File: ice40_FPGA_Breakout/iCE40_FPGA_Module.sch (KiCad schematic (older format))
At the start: 100 parts, among them U1 iCE40HX8_CT256

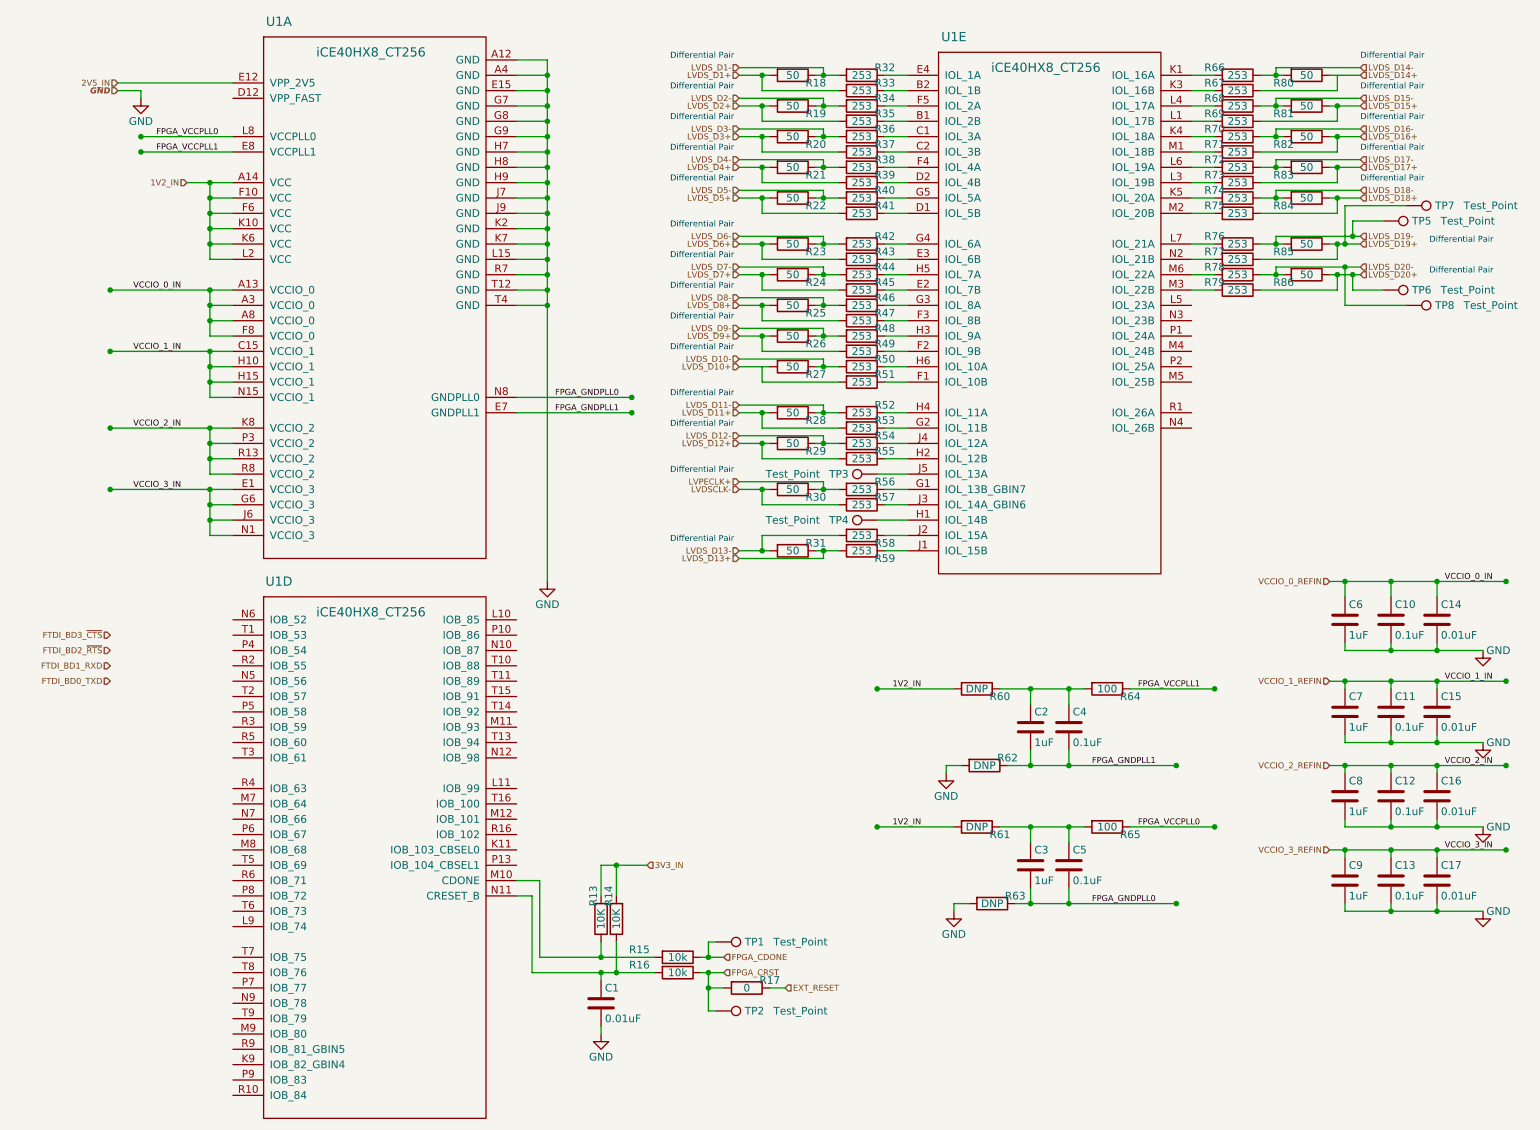
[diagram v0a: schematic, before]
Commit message: schematic clean up, label aligned
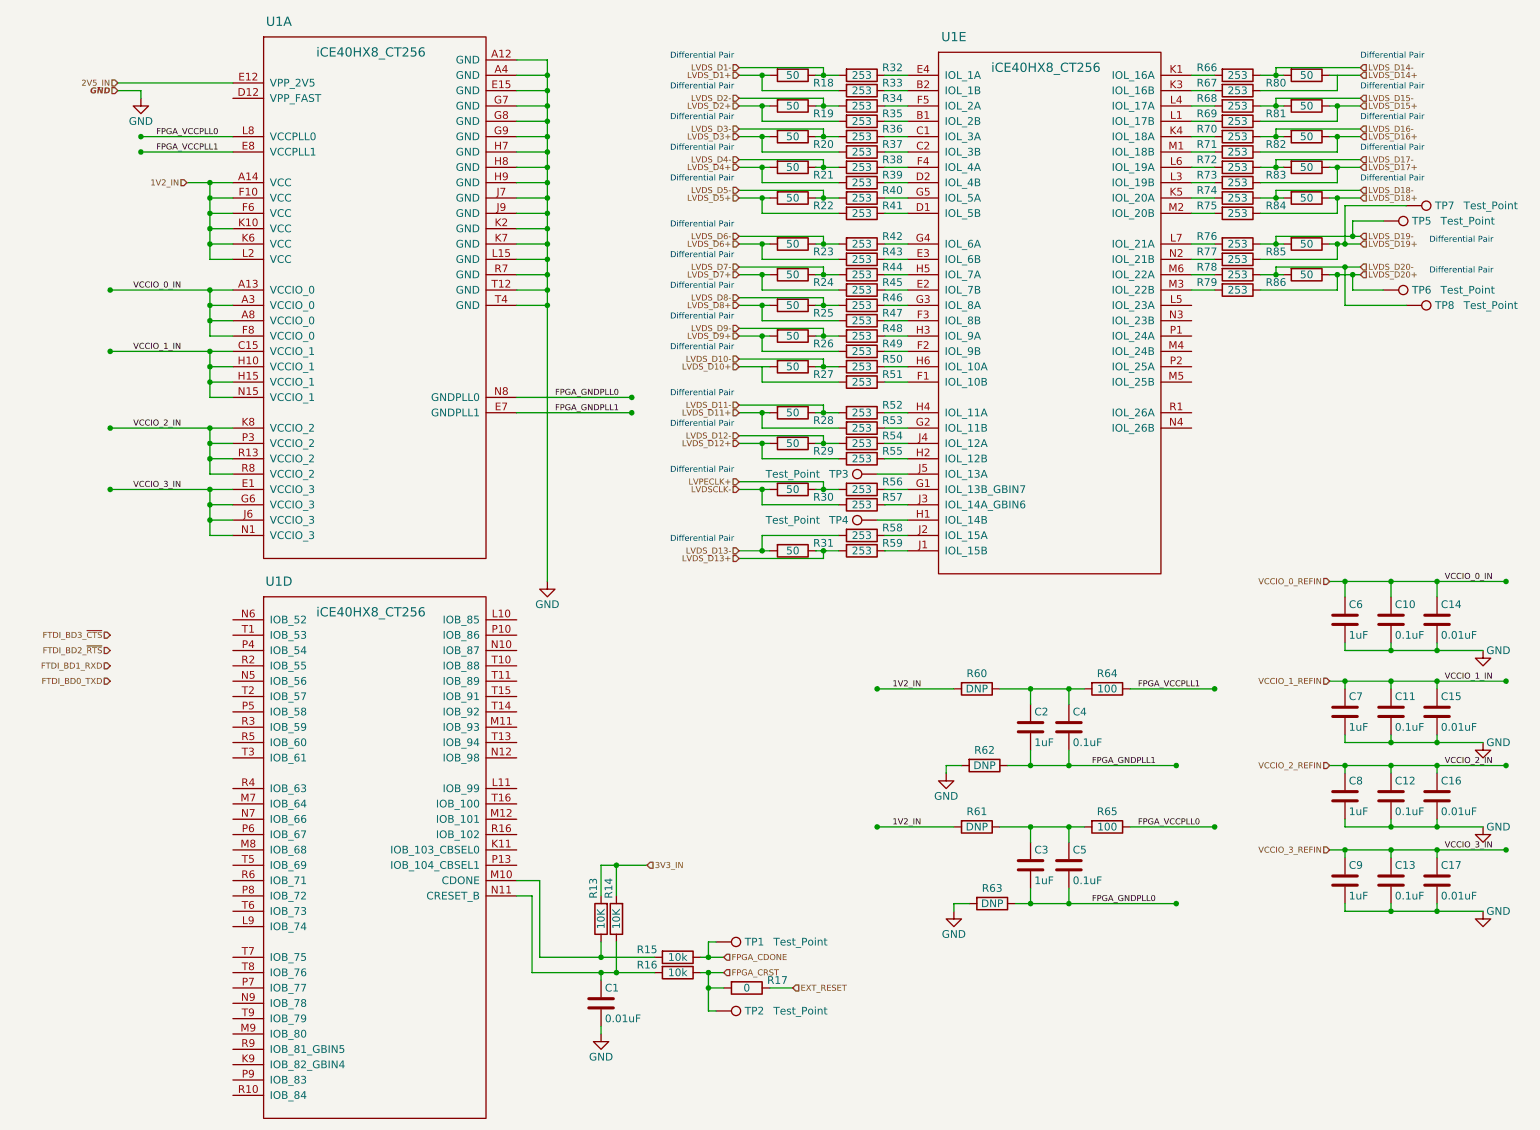
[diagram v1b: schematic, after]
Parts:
- C1, C10, C11, C12, C13, C14, C15, C16, C17, C4, C5: footprint (none) -> Capacitor_SMD:C_0402_1005Metric
- C2, C3, C6, C7, C8, C9: footprint (none) -> Capacitor_SMD:C_0603_1608Metric
- R13, R14, R15, R16, R17, R18, R19, R20, R21, R22, R23, R24, R25, R26, R27, R28, R29, R30, R31, R32, R33, R34, R35, R36, R37, R38, R39, R40, R41, R42, R43, R44, R45, R46, R47, R48, R49, R50, R51, R52, R53, R54, R55, R56, R57, R58, R59, R66, R67, R68, R69, R70, R71, R72, R73, R74, R75, R76, R77, R78, R79, R80, R81, R82, R83, R84, R85, R86: footprint (none) -> Resistor_SMD:R_0402_1005Metric
- R60, R61, R62, R63, R64, R65: footprint (none) -> Resistor_SMD:R_0603_1608Metric
- TP1, TP2, TP3, TP4, TP5, TP6, TP7, TP8: footprint (none) -> Conn_PinHeader_2.00mm:PinHeader_1x01_P2.00mm_Vertical

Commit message: assigned footprint to each component
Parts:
- TP1: footprint Conn_PinHeader_2.00mm:PinHeader_1x01_P2.00mm_Vertical -> TestPoint:TestPoint_Plated_Hole_D2.0mm
- TP2, TP3, TP4, TP5, TP6, TP7, TP8: footprint Conn_PinHeader_2.00mm:PinHeader_1x01_P2.00mm_Vertical -> TestPoint:TestPoint_Pad_D2.0mm
- U1: footprint (none) -> GTI_Footprint_Lib:BGA-256_12mmx12mm_Layout_14mmx14mm_P0.8mm_R0.5mm
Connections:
- net LVDS_D14+: now also R67.1

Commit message: , diff pair, memory and power component grouping
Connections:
- net LVDS_D10+: now also R51.2
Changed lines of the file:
@@
 $EndComp
 $Comp
-L GND #PWR02
+L GND #PWR3
 U 1 1 5A263712
 P 4800 4150
-F 0 "#PWR02" H 4800 3900 50  0001 C CNN
+F 0 "#PWR3" H 4800 3900 50  0001 C CNN
 F 1 "GND" H 4800 4000 50  0000 C CNN
 F 2 "" H 4800 4150 50  0001 C CNN
@@
 $EndComp
 $Comp
-L GND #PWR03
+L GND #PWR6
 U 1 1 5A3E2FC7
 P 7450 6300
-F 0 "#PWR03" H 7450 6050 50  0001 C CNN
+F 0 "#PWR6" H 7450 6050 50  0001 C CNN
 F 1 "GND" H 7450 6150 50  0000 C CNN
 F 2 "" H 7450 6300 50  0001 C CNN
@@
 $EndComp
 $Comp
-L GND #PWR04
+L GND #PWR5
 U 1 1 5A3E512A
 P 7400 5400
-F 0 "#PWR04" H 7400 5150 50  0001 C CNN
+F 0 "#PWR5" H 7400 5150 50  0001 C CNN
 F 1 "GND" H 7400 5250 50  0000 C CNN
 F 2 "" H 7400 5400 50  0001 C CNN
@@
 $EndComp
 $Comp
-L GND #PWR05
+L GND #PWR10
 U 1 1 5A407417
 P 10900 6300
-F 0 "#PWR05" H 10900 6050 50  0001 C CNN
+F 0 "#PWR10" H 10900 6050 50  0001 C CNN
 F 1 "GND" H 11000 6300 50  0000 C CNN
 F 2 "" H 10900 6300 50  0001 C CNN
@@
 $EndComp
 $Comp
-L GND #PWR06
+L GND #PWR8
 U 1 1 5A40791C
 P 10900 5200
-F 0 "#PWR06" H 10900 4950 50  0001 C CNN
+F 0 "#PWR8" H 10900 4950 50  0001 C CNN
 F 1 "GND" H 11000 5200 50  0000 C CNN
 F 2 "" H 10900 5200 50  0001 C CNN
@@
 $EndComp
 $Comp
-L GND #PWR07
+L GND #PWR7
 U 1 1 5A407BD5
 P 10900 4600
-F 0 "#PWR07" H 10900 4350 50  0001 C CNN
+F 0 "#PWR7" H 10900 4350 50  0001 C CNN
 F 1 "GND" H 11000 4600 50  0000 C CNN
 F 2 "" H 10900 4600 50  0001 C CNN
@@
 $EndComp
 $Comp
-L GND #PWR08
+L GND #PWR9
 U 1 1 5A407D06
 P 10900 5750
-F 0 "#PWR08" H 10900 5500 50  0001 C CNN
+F 0 "#PWR9" H 10900 5500 50  0001 C CNN
 F 1 "GND" H 11000 5750 50  0000 C CNN
 F 2 "" H 10900 5750 50  0001 C CNN
@@
 	6200 2850 6200 2750
 Wire Wire Line
-	6250 2750 6050 2750
+	6050 2750 6250 2750
 Wire Wire Line
 	6600 2750 6600 2700
@@
 	5150 7050 5150 7100
 $Comp
-L GND #PWR09
+L GND #PWR4
 U 1 1 5A2D5A99
 P 5150 7100
-F 0 "#PWR09" H 5150 6850 50  0001 C CNN
+F 0 "#PWR4" H 5150 6850 50  0001 C CNN
 F 1 "GND" H 5150 6950 50  0000 C CNN
 F 2 "" H 5150 7100 50  0001 C CNN
@@
 VCCIO_0_REFIN
 $Comp
-L GND #PWR010
+L GND #PWR2
 U 1 1 5A39D4DE
 P 2150 1000
-F 0 "#PWR010" H 2150 750 50  0001 C CNN
+F 0 "#PWR2" H 2150 750 50  0001 C CNN
 F 1 "GND" H 2150 850 50  0000 C CNN
 F 2 "" H 2150 1000 50  0001 C CNN
@@
 Differential Pair
 Connection ~ 9950 850
+Connection ~ 6200 2750
 $EndSCHEMATC

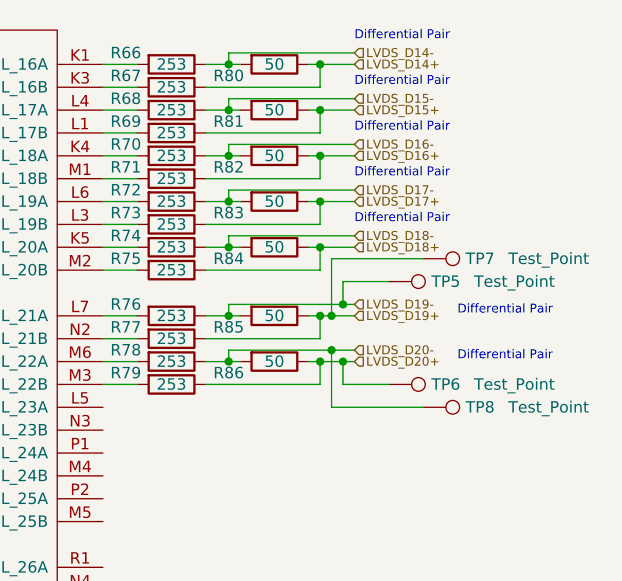
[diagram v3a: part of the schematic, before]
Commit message: update differential pair connection in schematic and updating layout placement for diff pair
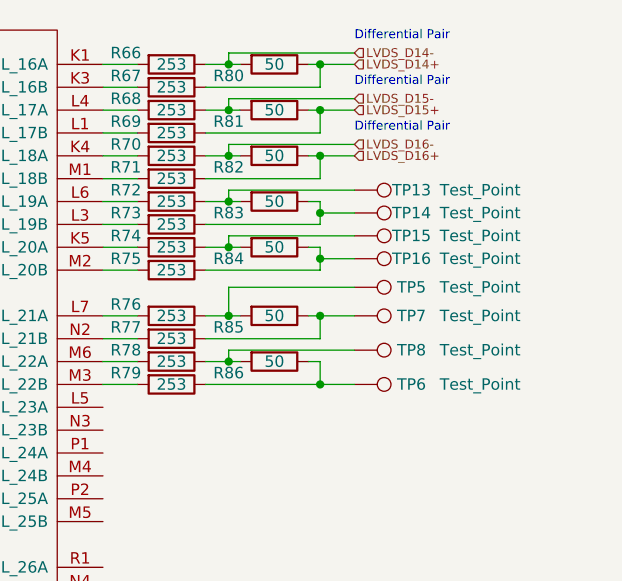
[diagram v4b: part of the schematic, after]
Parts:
- added TP13, TP14, TP15, TP16: Test_Point, TestPoint:TestPoint_THTPad_D1.0mm_Drill0.5mm, symbol Test_Point
- TP5, TP6, TP7, TP8: footprint TestPoint:TestPoint_Pad_D2.0mm -> TestPoint:TestPoint_THTPad_D1.0mm_Drill0.5mm
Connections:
- net LVDS_D17+: no longer names the net of R73.1, R83.1
- net LVDS_D17+: now also TP14.1
- net LVDS_D17-: no longer names the net of R72.1, R83.2
- net LVDS_D17-: now also TP13.1
- net LVDS_D18+: no longer names the net of R75.1, R84.1
- net LVDS_D18+: now also TP16.1
- net LVDS_D18-: no longer names the net of R74.1, R84.2
- net LVDS_D18-: now also TP15.1
- net LVDS_D19+: no longer names the net of R77.1, R85.1, TP7.1
- net LVDS_D19-: no longer names the net of R76.1, R85.2, TP5.1
- net LVDS_D20+: no longer names the net of R79.1, R86.1, TP6.1
- net LVDS_D20-: no longer names the net of R78.1, R86.2, TP8.1
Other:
- moved on the sheet: TP5, TP6, TP7, TP8
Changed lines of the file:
@@
 $Descr A4 11693 8268
 encoding utf-8
-Sheet 2 7
+Sheet 7 7
 Title ""
 Date ""
@@
 $EndComp
 $Comp
-L GND #PWR3
+L GND #PWR044
 U 1 1 5A263712
 P 4800 4150
-F 0 "#PWR3" H 4800 3900 50  0001 C CNN
+F 0 "#PWR044" H 4800 3900 50  0001 C CNN
 F 1 "GND" H 4800 4000 50  0000 C CNN
 F 2 "" H 4800 4150 50  0001 C CNN
@@
 L Test_Point TP5
 U 1 1 5A3B7D9A
-P 10250 1800
-F 0 "TP5" V 10250 2050 50  0000 C CNN
-F 1 "Test_Point" V 10250 2350 50  0000 C CNN
-F 2 "TestPoint:TestPoint_Pad_D2.0mm" H 10450 1800 50  0001 C CNN
-F 3 "" H 10450 1800 50  0001 C CNN
-	1    10250 1800
+P 10100 1825
+F 0 "TP5" V 10100 2075 50  0000 C CNN
+F 1 "Test_Point" V 10100 2375 50  0000 C CNN
+F 2 "TestPoint:TestPoint_THTPad_D1.0mm_Drill0.5mm" H 10300 1825 50  0001 C CNN
+F 3 "" H 10300 1825 50  0001 C CNN
+	1    10100 1825
 	0    1    1    0
 $EndComp
@@
 L Test_Point TP7
 U 1 1 5A3B7DA1
-P 10400 1700
-F 0 "TP7" V 10400 1950 50  0000 C CNN
-F 1 "Test_Point" V 10400 2250 50  0000 C CNN
-F 2 "TestPoint:TestPoint_Pad_D2.0mm" H 10600 1700 50  0001 C CNN
-F 3 "" H 10600 1700 50  0001 C CNN
-	1    10400 1700
+P 10100 1950
+F 0 "TP7" V 10100 2200 50  0000 C CNN
+F 1 "Test_Point" V 10100 2500 50  0000 C CNN
+F 2 "TestPoint:TestPoint_THTPad_D1.0mm_Drill0.5mm" H 10300 1950 50  0001 C CNN
+F 3 "" H 10300 1950 50  0001 C CNN
+	1    10100 1950
 	0    1    1    0
 $EndComp
@@
 L Test_Point TP6
 U 1 1 5A3B7DA8
-P 10250 2250
-F 0 "TP6" V 10250 2500 50  0000 C CNN
-F 1 "Test_Point" V 10250 2800 50  0000 C CNN
-F 2 "TestPoint:TestPoint_Pad_D2.0mm" H 10450 2250 50  0001 C CNN
-F 3 "" H 10450 2250 50  0001 C CNN
-	1    10250 2250
+P 10100 2250
+F 0 "TP6" V 10100 2500 50  0000 C CNN
+F 1 "Test_Point" V 10100 2800 50  0000 C CNN
+F 2 "TestPoint:TestPoint_THTPad_D1.0mm_Drill0.5mm" H 10300 2250 50  0001 C CNN
+F 3 "" H 10300 2250 50  0001 C CNN
+	1    10100 2250
 	0    1    1    0
 $EndComp
@@
 L Test_Point TP8
 U 1 1 5A3B7DAF
-P 10400 2350
-F 0 "TP8" V 10400 2600 50  0000 C CNN
-F 1 "Test_Point" V 10400 2900 50  0000 C CNN
-F 2 "TestPoint:TestPoint_Pad_D2.0mm" H 10600 2350 50  0001 C CNN
-F 3 "" H 10600 2350 50  0001 C CNN
-	1    10400 2350
+P 10100 2100
+F 0 "TP8" V 10100 2350 50  0000 C CNN
+F 1 "Test_Point" V 10100 2650 50  0000 C CNN
+F 2 "TestPoint:TestPoint_THTPad_D1.0mm_Drill0.5mm" H 10300 2100 50  0001 C CNN
+F 3 "" H 10300 2100 50  0001 C CNN
+	1    10100 2100
 	0    1    1    0
 $EndComp
@@
 $EndComp
 $Comp
-L GND #PWR6
+L GND #PWR045
 U 1 1 5A3E2FC7
 P 7450 6300
-F 0 "#PWR6" H 7450 6050 50  0001 C CNN
+F 0 "#PWR045" H 7450 6050 50  0001 C CNN
 F 1 "GND" H 7450 6150 50  0000 C CNN
 F 2 "" H 7450 6300 50  0001 C CNN
@@
 $EndComp
 $Comp
-L GND #PWR5
+L GND #PWR046
 U 1 1 5A3E512A
 P 7400 5400
-F 0 "#PWR5" H 7400 5150 50  0001 C CNN
+F 0 "#PWR046" H 7400 5150 50  0001 C CNN
 F 1 "GND" H 7400 5250 50  0000 C CNN
 F 2 "" H 7400 5400 50  0001 C CNN
@@
 $EndComp
 $Comp
-L GND #PWR10
+L GND #PWR047
 U 1 1 5A407417
 P 10900 6300
-F 0 "#PWR10" H 10900 6050 50  0001 C CNN
+F 0 "#PWR047" H 10900 6050 50  0001 C CNN
 F 1 "GND" H 11000 6300 50  0000 C CNN
 F 2 "" H 10900 6300 50  0001 C CNN
@@
 $EndComp
 $Comp
-L GND #PWR8
+L GND #PWR048
 U 1 1 5A40791C
 P 10900 5200
-F 0 "#PWR8" H 10900 4950 50  0001 C CNN
+F 0 "#PWR048" H 10900 4950 50  0001 C CNN
 F 1 "GND" H 11000 5200 50  0000 C CNN
 F 2 "" H 10900 5200 50  0001 C CNN
@@
 $EndComp
 $Comp
-L GND #PWR7
+L GND #PWR049
 U 1 1 5A407BD5
 P 10900 4600
-F 0 "#PWR7" H 10900 4350 50  0001 C CNN
+F 0 "#PWR049" H 10900 4350 50  0001 C CNN
 F 1 "GND" H 11000 4600 50  0000 C CNN
 F 2 "" H 10900 4600 50  0001 C CNN
@@
 $EndComp
 $Comp
-L GND #PWR9
+L GND #PWR050
 U 1 1 5A407D06
 P 10900 5750
-F 0 "#PWR9" H 10900 5500 50  0001 C CNN
+F 0 "#PWR050" H 10900 5500 50  0001 C CNN
 F 1 "GND" H 11000 5750 50  0000 C CNN
 F 2 "" H 10900 5750 50  0001 C CNN
@@
 	9450 1650 9600 1650
 Wire Wire Line
-	9450 1750 9950 1750
-Wire Wire Line
-	9950 1750 9950 1650
-Wire Wire Line
-	9900 1650 10100 1650
-Connection ~ 9950 1650
+	9950 1750 9450 1750
+Wire Wire Line
+	9950 1650 9950 1750
+Wire Wire Line
+	9950 1650 9900 1650
 Wire Wire Line
 	9550 1650 9550 1600
-Wire Wire Line
-	9550 1600 10100 1600
 Connection ~ 9550 1650
 Wire Wire Line
 	9450 1450 9600 1450
 Wire Wire Line
-	9450 1550 9950 1550
-Wire Wire Line
-	9950 1550 9950 1450
-Wire Wire Line
-	9900 1450 10100 1450
-Connection ~ 9950 1450
+	9950 1550 9450 1550
+Wire Wire Line
+	9950 1450 9950 1550
 Wire Wire Line
 	9550 1450 9550 1400
@@
 Wire Wire Line
 	9950 2050 9950 1950
-Wire Wire Line
-	9900 1950 10100 1950
 Connection ~ 9950 1950
 Wire Wire Line
 	9450 2150 9600 2150
 Wire Wire Line
-	9450 2250 9950 2250
+	9450 2250 10100 2250
 Wire Wire Line
 	9950 2250 9950 2150
 Wire Wire Line
-	9900 2150 10100 2150
-Connection ~ 9950 2150
-Wire Wire Line
-	9550 1900 10100 1900
-Wire Wire Line
-	9550 1900 9550 1950
+	9550 1825 9550 1950
 Connection ~ 9550 1950
-Wire Wire Line
-	9550 2100 10100 2100
 Wire Wire Line
 	9550 2100 9550 2150
 Connection ~ 9550 2150
 Wire Wire Line
-	10250 2250 10050 2250
-Wire Wire Line
-	10050 2250 10050 2150
-Connection ~ 10050 2150
-Wire Wire Line
-	10400 2350 10000 2350
-Wire Wire Line
-	10000 2350 10000 2100
-Connection ~ 10000 2100
-Wire Wire Line
-	10250 1800 10050 1800
-Wire Wire Line
-	10050 1800 10050 1900
-Connection ~ 10050 1900
-Wire Wire Line
-	10400 1700 10000 1700
-Wire Wire Line
-	10000 1700 10000 1950
-Connection ~ 10000 1950
+	9550 2100 10100 2100
+Wire Wire Line
+	9550 1825 10100 1825
+Wire Wire Line
+	9900 1950 10100 1950
 Wire Wire Line
 	6550 3550 6700 3550
@@
 	5150 7050 5150 7100
 $Comp
-L GND #PWR4
+L GND #PWR051
 U 1 1 5A2D5A99
 P 5150 7100
-F 0 "#PWR4" H 5150 6850 50  0001 C CNN
+F 0 "#PWR051" H 5150 6850 50  0001 C CNN
 F 1 "GND" H 5150 6950 50  0000 C CNN
 F 2 "" H 5150 7100 50  0001 C CNN
@@
 Text HLabel 10100 1250 2    39   Input ~ 0
 LVDS_D16+
-Text HLabel 10100 1400 2    39   Input ~ 0
-LVDS_D17-
-Text HLabel 10100 1450 2    39   Input ~ 0
-LVDS_D17+
-Text HLabel 10100 1600 2    39   Input ~ 0
-LVDS_D18-
-Text HLabel 10100 1650 2    39   Input ~ 0
-LVDS_D18+
-Text HLabel 10100 1900 2    39   Input ~ 0
-LVDS_D19-
-Text HLabel 10100 1950 2    39   Input ~ 0
-LVDS_D19+
-Text HLabel 10100 2100 2    39   Input ~ 0
-LVDS_D20-
-Text HLabel 10100 2150 2    39   Input ~ 0
-LVDS_D20+
 Text HLabel 9900 4800 0    39   Input ~ 0
 VCCIO_1_REFIN
@@
 VCCIO_0_REFIN
 $Comp
-L GND #PWR2
+L GND #PWR052
 U 1 1 5A39D4DE
 P 2150 1000
-F 0 "#PWR2" H 2150 750 50  0001 C CNN
+F 0 "#PWR052" H 2150 750 50  0001 C CNN
 F 1 "GND" H 2150 850 50  0000 C CNN
 F 2 "" H 2150 1000 50  0001 C CNN
@@
 Text Notes 10100 1150 0    39   ~ 0
 Differential Pair
-Text Notes 10100 1350 0    39   ~ 0
-Differential Pair
-Text Notes 10100 1550 0    39   ~ 0
-Differential Pair
-Text Notes 10550 1950 0    39   ~ 0
-Differential Pair
-Text Notes 10550 2150 0    39   ~ 0
-Differential Pair
 Connection ~ 9950 850
 Connection ~ 6200 2750
+Wire Wire Line
+	9950 1450 9900 1450
+Wire Wire Line
+	9550 1600 10100 1600
+Wire Wire Line
+	9950 2150 9900 2150
+Connection ~ 9950 2250
+$Comp
+L Test_Point TP13
+U 1 1 5AD8C648
+P 10100 1400
+F 0 "TP13" V 10100 1650 50  0000 C CNN
+F 1 "Test_Point" V 10100 1950 50  0000 C CNN
+F 2 "TestPoint:TestPoint_THTPad_D1.0mm_Drill0.5mm" H 10300 1400 50  0001 C CNN
+F 3 "" H 10300 1400 50  0001 C CNN
+	1    10100 1400
+	0    1    1    0
+$EndComp
+$Comp
+L Test_Point TP14
+U 1 1 5AD8C7B9
+P 10100 1500
+F 0 "TP14" V 10100 1750 50  0000 C CNN
+F 1 "Test_Point" V 10100 2050 50  0000 C CNN
+F 2 "TestPoint:TestPoint_THTPad_D1.0mm_Drill0.5mm" H 10300 1500 50  0001 C CNN
+F 3 "" H 10300 1500 50  0001 C CNN
+	1    10100 1500
+	0    1    1    0
+$EndComp
+$Comp
+L Test_Point TP15
+U 1 1 5AD8C90D
+P 10100 1600
+F 0 "TP15" V 10100 1850 50  0000 C CNN
+F 1 "Test_Point" V 10100 2150 50  0000 C CNN
+F 2 "TestPoint:TestPoint_THTPad_D1.0mm_Drill0.5mm" H 10300 1600 50  0001 C CNN
+F 3 "" H 10300 1600 50  0001 C CNN
+	1    10100 1600
+	0    1    1    0
+$EndComp
+$Comp
+L Test_Point TP16
+U 1 1 5AD8CA62
+P 10100 1700
+F 0 "TP16" V 10100 1950 50  0000 C CNN
+F 1 "Test_Point" V 10100 2250 50  0000 C CNN
+F 2 "TestPoint:TestPoint_THTPad_D1.0mm_Drill0.5mm" H 10300 1700 50  0001 C CNN
+F 3 "" H 10300 1700 50  0001 C CNN
+	1    10100 1700
+	0    1    1    0
+$EndComp
+Wire Wire Line
+	10100 1500 9950 1500
+Connection ~ 9950 1500
+Wire Wire Line
+	10100 1700 9950 1700
+Connection ~ 9950 1700
 $EndSCHEMATC
